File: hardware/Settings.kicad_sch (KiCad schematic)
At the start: 4 parts

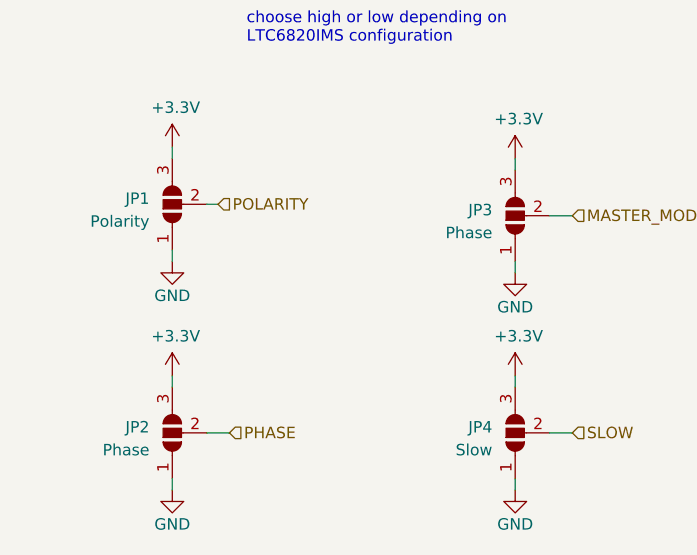
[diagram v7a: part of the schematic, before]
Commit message: hardware update - fixed pcb errors
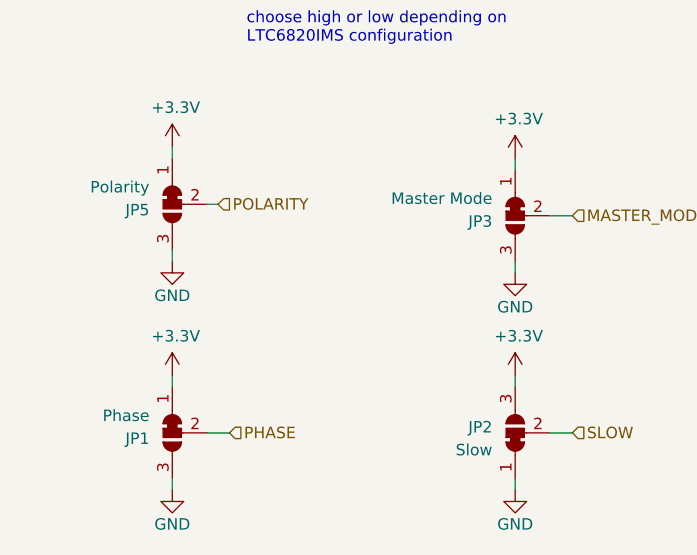
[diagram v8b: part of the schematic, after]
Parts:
- removed JP1: Polarity, Jumper:SolderJumper-3_P2.0mm_Open_TrianglePad1.0x1.5mm_NumberLabels, symbol Jumper:SolderJumper_3_Open
- removed JP2, JP3: Phase, Jumper:SolderJumper-3_P2.0mm_Open_TrianglePad1.0x1.5mm_NumberLabels, symbol Jumper:SolderJumper_3_Open
- removed JP4: Slow, Jumper:SolderJumper-3_P2.0mm_Open_TrianglePad1.0x1.5mm_NumberLabels, symbol Jumper:SolderJumper_3_Open
- added JP1: Phase, Jumper:SolderJumper-3_P1.3mm_Bridged12_RoundedPad1.0x1.5mm, symbol Jumper:SolderJumper_3_Bridged12
- added JP2: Slow, Jumper:SolderJumper-3_P1.3mm_Bridged12_RoundedPad1.0x1.5mm, symbol Jumper:SolderJumper_3_Bridged12
- added JP3: Master Mode, Jumper:SolderJumper-3_P1.3mm_Bridged12_RoundedPad1.0x1.5mm, symbol Jumper:SolderJumper_3_Bridged12
- added JP5: Polarity, Jumper:SolderJumper-3_P1.3mm_Bridged12_RoundedPad1.0x1.5mm, symbol Jumper:SolderJumper_3_Bridged12
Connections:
- net +3V3: now also JP1.1 (A), JP2.3 (B), JP3.1 (A), JP5.1 (A)
- net GND: now also JP1.3 (B), JP2.1 (A), JP3.3 (B), JP5.3 (B)
- net MASTER_MODE: now also JP3.2 (C)
- net PHASE: now also JP1.2 (C)
- net POLARITY: now also JP5.2 (C)
- net SLOW: now also JP2.2 (C)
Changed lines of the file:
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@@
     (effects (font (size 1.27 1.27)) (justify left))
   )
-  (symbol (lib_id "Jumper:SolderJumper_3_Open") (at 63.5 92.71 90) (unit 1)
-    (in_bom yes) (on_board yes) (dnp no) (fields_autoplaced)
-    (property "Reference" "JP2" (at 60.96 92.075 90)
-      (effects (font (size 1.27 1.27)) (justify left))
-    )
-    (property "Value" "Phase" (at 60.96 94.615 90)
-      (effects (font (size 1.27 1.27)) (justify left))
-    )
-    (property "Footprint" "Jumper:SolderJumper-3_P2.0mm_Open_TrianglePad1.0x1.5mm_NumberLabels" (at 63.5 92.71 0)
+  (symbol (lib_id "Jumper:SolderJumper_3_Bridged12") (at 63.5 92.71 90) (mirror x) (unit 1)
+    (in_bom yes) (on_board yes) (dnp no)
+    (property "Reference" "JP1" (at 60.96 93.345 90)
+      (effects (font (size 1.27 1.27)) (justify left))
+    )
+    (property "Value" "Phase" (at 60.96 90.805 90)
+      (effects (font (size 1.27 1.27)) (justify left))
+    )
+    (property "Footprint" "Jumper:SolderJumper-3_P1.3mm_Bridged12_RoundedPad1.0x1.5mm" (at 63.5 92.71 0)
       (effects (font (size 1.27 1.27)) hide)
     )
@@
       (project "PUTM_EV_BMS_HV_Master_2021"
         (path "/b456cffc-d9d7-4c91-91f2-36ec9a65dd1b/d3d45b10-2d5f-4953-9ccf-4b0c82a2ee03"
+          (reference "JP1") (unit 1)
+        )
+      )
+    )
+  )
+  (symbol (lib_id "power:GND") (at 63.5 73.66 0) (unit 1)
+    (in_bom yes) (on_board yes) (dnp no)
+    (property "Reference" "#PWR02" (at 63.5 80.01 0)
+      (effects (font (size 1.27 1.27)) hide)
+    )
+    (property "Value" "GND" (at 63.5 77.47 0)
+      (effects (font (size 1.27 1.27)))
+    )
+    (property "Footprint" "" (at 63.5 73.66 0)
+      (effects (font (size 1.27 1.27)) hide)
+    )
+    (property "Datasheet" "" (at 63.5 73.66 0)
+      (effects (font (size 1.27 1.27)) hide)
+    )
+    (pin "1")
+    (instances
+      (project "PUTM_EV_BMS_HV_Master_2021"
+        (path "/b456cffc-d9d7-4c91-91f2-36ec9a65dd1b/d3d45b10-2d5f-4953-9ccf-4b0c82a2ee03"
+          (reference "#PWR02") (unit 1)
+        )
+      )
+    )
+  )
+  (symbol (lib_id "power:+3.3V") (at 101.6 62.23 0) (unit 1)
+    (in_bom yes) (on_board yes) (dnp no)
+    (property "Reference" "#PWR06" (at 101.6 66.04 0)
+      (effects (font (size 1.27 1.27)) hide)
+    )
+    (property "Value" "+3.3V" (at 101.981 57.8358 0)
+      (effects (font (size 1.27 1.27)))
+    )
+    (property "Footprint" "" (at 101.6 62.23 0)
+      (effects (font (size 1.27 1.27)) hide)
+    )
+    (property "Datasheet" "" (at 101.6 62.23 0)
+      (effects (font (size 1.27 1.27)) hide)
+    )
+    (pin "1")
+    (instances
+      (project "PUTM_EV_BMS_HV_Master_2021"
+        (path "/b456cffc-d9d7-4c91-91f2-36ec9a65dd1b/d3d45b10-2d5f-4953-9ccf-4b0c82a2ee03"
+          (reference "#PWR06") (unit 1)
+        )
+      )
+    )
+  )
+  (symbol (lib_id "Jumper:SolderJumper_3_Bridged12") (at 101.6 92.71 90) (unit 1)
+    (in_bom yes) (on_board yes) (dnp no)
+    (property "Reference" "JP2" (at 99.06 92.075 90)
+      (effects (font (size 1.27 1.27)) (justify left))
+    )
+    (property "Value" "Slow" (at 99.06 94.615 90)
+      (effects (font (size 1.27 1.27)) (justify left))
+    )
+    (property "Footprint" "Jumper:SolderJumper-3_P1.3mm_Bridged12_RoundedPad1.0x1.5mm" (at 133.35 87.63 0)
+      (effects (font (size 1.27 1.27)) hide)
+    )
+    (property "Datasheet" "~" (at 101.6 92.71 0)
+      (effects (font (size 1.27 1.27)) hide)
+    )
+    (pin "1")
+    (pin "2")
+    (pin "3")
+    (instances
+      (project "PUTM_EV_BMS_HV_Master_2021"
+        (path "/b456cffc-d9d7-4c91-91f2-36ec9a65dd1b/d3d45b10-2d5f-4953-9ccf-4b0c82a2ee03"
           (reference "JP2") (unit 1)
         )
@@
     )
   )
-  (symbol (lib_id "power:GND") (at 63.5 73.66 0) (unit 1)
-    (in_bom yes) (on_board yes) (dnp no)
-    (property "Reference" "#PWR02" (at 63.5 80.01 0)
-      (effects (font (size 1.27 1.27)) hide)
-    )
-    (property "Value" "GND" (at 63.5 77.47 0)
-      (effects (font (size 1.27 1.27)))
-    )
-    (property "Footprint" "" (at 63.5 73.66 0)
-      (effects (font (size 1.27 1.27)) hide)
-    )
-    (property "Datasheet" "" (at 63.5 73.66 0)
-      (effects (font (size 1.27 1.27)) hide)
-    )
-    (pin "1")
-    (instances
-      (project "PUTM_EV_BMS_HV_Master_2021"
-        (path "/b456cffc-d9d7-4c91-91f2-36ec9a65dd1b/d3d45b10-2d5f-4953-9ccf-4b0c82a2ee03"
-          (reference "#PWR02") (unit 1)
-        )
-      )
-    )
-  )
-  (symbol (lib_id "power:+3.3V") (at 101.6 62.23 0) (unit 1)
-    (in_bom yes) (on_board yes) (dnp no)
-    (property "Reference" "#PWR06" (at 101.6 66.04 0)
-      (effects (font (size 1.27 1.27)) hide)
-    )
-    (property "Value" "+3.3V" (at 101.981 57.8358 0)
-      (effects (font (size 1.27 1.27)))
-    )
-    (property "Footprint" "" (at 101.6 62.23 0)
-      (effects (font (size 1.27 1.27)) hide)
-    )
-    (property "Datasheet" "" (at 101.6 62.23 0)
-      (effects (font (size 1.27 1.27)) hide)
-    )
-    (pin "1")
-    (instances
-      (project "PUTM_EV_BMS_HV_Master_2021"
-        (path "/b456cffc-d9d7-4c91-91f2-36ec9a65dd1b/d3d45b10-2d5f-4953-9ccf-4b0c82a2ee03"
-          (reference "#PWR06") (unit 1)
-        )
-      )
-    )
-  )
   (symbol (lib_id "power:GND") (at 101.6 99.06 0) (unit 1)
     (in_bom yes) (on_board yes) (dnp no)
@@
     )
   )
+  (symbol (lib_id "Jumper:SolderJumper_3_Bridged12") (at 101.6 68.58 90) (mirror x) (unit 1)
+    (in_bom yes) (on_board yes) (dnp no)
+    (property "Reference" "JP3" (at 99.06 69.215 90)
+      (effects (font (size 1.27 1.27)) (justify left))
+    )
+    (property "Value" "Master Mode" (at 99.06 66.675 90)
+      (effects (font (size 1.27 1.27)) (justify left))
+    )
+    (property "Footprint" "Jumper:SolderJumper-3_P1.3mm_Bridged12_RoundedPad1.0x1.5mm" (at 101.6 68.58 0)
+      (effects (font (size 1.27 1.27)) hide)
+    )
+    (property "Datasheet" "~" (at 101.6 68.58 0)
+      (effects (font (size 1.27 1.27)) hide)
+    )
+    (pin "1")
+    (pin "2")
+    (pin "3")
+    (instances
+      (project "PUTM_EV_BMS_HV_Master_2021"
+        (path "/b456cffc-d9d7-4c91-91f2-36ec9a65dd1b/d3d45b10-2d5f-4953-9ccf-4b0c82a2ee03"
+          (reference "JP3") (unit 1)
+        )
+      )
+    )
+  )
   (symbol (lib_id "power:+3.3V") (at 63.5 86.36 0) (unit 1)
     (in_bom yes) (on_board yes) (dnp no)
@@
     )
   )
-  (symbol (lib_id "Jumper:SolderJumper_3_Open") (at 101.6 92.71 90) (unit 1)
-    (in_bom yes) (on_board yes) (dnp no) (fields_autoplaced)
-    (property "Reference" "JP4" (at 99.06 92.075 90)
-      (effects (font (size 1.27 1.27)) (justify left))
-    )
-    (property "Value" "Slow" (at 99.06 94.615 90)
-      (effects (font (size 1.27 1.27)) (justify left))
-    )
-    (property "Footprint" "Jumper:SolderJumper-3_P2.0mm_Open_TrianglePad1.0x1.5mm_NumberLabels" (at 101.6 92.71 0)
-      (effects (font (size 1.27 1.27)) hide)
-    )
-    (property "Datasheet" "~" (at 101.6 92.71 0)
-      (effects (font (size 1.27 1.27)) hide)
-    )
-    (pin "1")
-    (pin "2")
-    (pin "3")
-    (instances
-      (project "PUTM_EV_BMS_HV_Master_2021"
-        (path "/b456cffc-d9d7-4c91-91f2-36ec9a65dd1b/d3d45b10-2d5f-4953-9ccf-4b0c82a2ee03"
-          (reference "JP4") (unit 1)
-        )
-      )
-    )
-  )
   (symbol (lib_id "power:GND") (at 101.6 74.93 0) (unit 1)
     (in_bom yes) (on_board yes) (dnp no)
@@
     )
   )
-  (symbol (lib_id "Jumper:SolderJumper_3_Open") (at 63.5 67.31 90) (unit 1)
-    (in_bom yes) (on_board yes) (dnp no) (fields_autoplaced)
-    (property "Reference" "JP1" (at 60.96 66.675 90)
-      (effects (font (size 1.27 1.27)) (justify left))
-    )
-    (property "Value" "Polarity" (at 60.96 69.215 90)
-      (effects (font (size 1.27 1.27)) (justify left))
-    )
-    (property "Footprint" "Jumper:SolderJumper-3_P2.0mm_Open_TrianglePad1.0x1.5mm_NumberLabels" (at 63.5 67.31 0)
+  (symbol (lib_id "Jumper:SolderJumper_3_Bridged12") (at 63.5 67.31 90) (mirror x) (unit 1)
+    (in_bom yes) (on_board yes) (dnp no)
+    (property "Reference" "JP5" (at 60.96 67.945 90)
+      (effects (font (size 1.27 1.27)) (justify left))
+    )
+    (property "Value" "Polarity" (at 60.96 65.405 90)
+      (effects (font (size 1.27 1.27)) (justify left))
+    )
+    (property "Footprint" "Jumper:SolderJumper-3_P1.3mm_Bridged12_RoundedPad1.0x1.5mm" (at 63.5 67.31 0)
       (effects (font (size 1.27 1.27)) hide)
     )
@@
       (project "PUTM_EV_BMS_HV_Master_2021"
         (path "/b456cffc-d9d7-4c91-91f2-36ec9a65dd1b/d3d45b10-2d5f-4953-9ccf-4b0c82a2ee03"
-          (reference "JP1") (unit 1)
-        )
-      )
-    )
-  )
-  (symbol (lib_id "Jumper:SolderJumper_3_Open") (at 101.6 68.58 90) (unit 1)
-    (in_bom yes) (on_board yes) (dnp no) (fields_autoplaced)
-    (property "Reference" "JP3" (at 99.06 67.945 90)
-      (effects (font (size 1.27 1.27)) (justify left))
-    )
-    (property "Value" "Phase" (at 99.06 70.485 90)
-      (effects (font (size 1.27 1.27)) (justify left))
-    )
-    (property "Footprint" "Jumper:SolderJumper-3_P2.0mm_Open_TrianglePad1.0x1.5mm_NumberLabels" (at 101.6 68.58 0)
-      (effects (font (size 1.27 1.27)) hide)
-    )
-    (property "Datasheet" "~" (at 101.6 68.58 0)
-      (effects (font (size 1.27 1.27)) hide)
-    )
-    (pin "1")
-    (pin "2")
-    (pin "3")
-    (instances
-      (project "PUTM_EV_BMS_HV_Master_2021"
-        (path "/b456cffc-d9d7-4c91-91f2-36ec9a65dd1b/d3d45b10-2d5f-4953-9ccf-4b0c82a2ee03"
-          (reference "JP3") (unit 1)
-        )
-      )
+          (reference "JP5") (unit 1)
+        )
+      )
